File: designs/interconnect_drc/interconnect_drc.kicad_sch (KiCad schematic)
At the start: 1 part

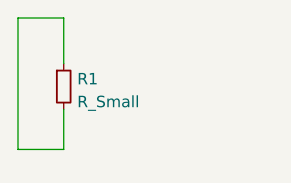
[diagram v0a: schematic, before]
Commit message: Convert to teardrop testcase
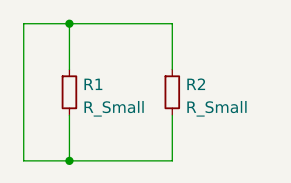
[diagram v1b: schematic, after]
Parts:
- added R2: R_Small, Resistor_SMD:R_0201_0603Metric_Pad0.64x0.40mm_HandSolder, symbol Device:R_Small
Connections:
- net at R1.1, R1.2: now also R2.1, R2.2
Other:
- moved on the sheet: R1
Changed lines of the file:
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@@
-(kicad_sch (version 20211123) (generator eeschema)
+(kicad_sch (version 20230121) (generator eeschema)
   (paper "A4")
-  (wire (pts (xy 93.345 112.395) (xy 93.345 127))
-    (stroke (width 0) (type default) (color 0 0 0 0))
+  (junction (at 99.06 113.03) (diameter 0) (color 0 0 0 0)
   )
-  (wire (pts (xy 98.425 117.475) (xy 98.425 112.395))
-    (stroke (width 0) (type default) (color 0 0 0 0))
+  (junction (at 99.06 128.27) (diameter 0) (color 0 0 0 0)
   )
-  (wire (pts (xy 98.425 112.395) (xy 93.345 112.395))
-    (stroke (width 0) (type default) (color 0 0 0 0))
+  (wire (pts (xy 99.06 113.03) (xy 110.49 113.03))
+    (stroke (width 0) (type default))
   )
-  (wire (pts (xy 98.425 127) (xy 98.425 122.555))
-    (stroke (width 0) (type default) (color 0 0 0 0))
+  (wire (pts (xy 110.49 123.19) (xy 110.49 128.27))
+    (stroke (width 0) (type default))
   )
-  (wire (pts (xy 93.345 127) (xy 98.425 127))
-    (stroke (width 0) (type default) (color 0 0 0 0))
+  (wire (pts (xy 110.49 128.27) (xy 99.06 128.27))
+    (stroke (width 0) (type default))
   )
-  (symbol (lib_id "Device:R_Small") (at 98.425 120.015 0) (unit 1)
-    (in_bom yes) (on_board yes) (fields_autoplaced)
-    (property "Reference" "R1" (id 0) (at 99.9236 119.1803 0)
+  (wire (pts (xy 110.49 113.03) (xy 110.49 118.11))
+    (stroke (width 0) (type default))
+  )
+  (wire (pts (xy 93.98 113.03) (xy 93.98 128.27))
+    (stroke (width 0) (type default))
+  )
+  (wire (pts (xy 99.06 118.11) (xy 99.06 113.03))
+    (stroke (width 0) (type default))
+  )
+  (wire (pts (xy 99.06 113.03) (xy 93.98 113.03))
+    (stroke (width 0) (type default))
+  )
+  (wire (pts (xy 99.06 128.27) (xy 99.06 123.19))
+    (stroke (width 0) (type default))
+  )
+  (wire (pts (xy 93.98 128.27) (xy 99.06 128.27))
+    (stroke (width 0) (type default))
+  )
+  (symbol (lib_id "Device:R_Small") (at 110.49 120.65 0) (unit 1)
+    (in_bom yes) (on_board yes) (dnp no) (fields_autoplaced)
+    (property "Reference" "R2" (at 111.9886 119.8153 0)
       (effects (font (size 1.27 1.27)) (justify left))
     )
-    (property "Value" "R_Small" (id 1) (at 99.9236 121.7172 0)
+    (property "Value" "R_Small" (at 111.9886 122.3522 0)
       (effects (font (size 1.27 1.27)) (justify left))
     )
-    (property "Footprint" "Resistor_SMD:R_0201_0603Metric_Pad0.64x0.40mm_HandSolder" (id 2) (at 98.425 120.015 0)
+    (property "Footprint" "Resistor_SMD:R_0201_0603Metric_Pad0.64x0.40mm_HandSolder" (at 110.49 120.65 0)
       (effects (font (size 1.27 1.27)) hide)
     )
-    (property "Datasheet" "~" (id 3) (at 98.425 120.015 0)
+    (property "Datasheet" "~" (at 110.49 120.65 0)
       (effects (font (size 1.27 1.27)) hide)
     )
     (pin "1")
     (pin "2")
+    (instances
+      (project "interconnect_drc"
+        (path "/0ce8ef0c-bf84-4f52-8da6-310f1efa5175"
+          (reference "R2") (unit 1)
+        )
+      )
+    )
+  )
+  (symbol (lib_id "Device:R_Small") (at 99.06 120.65 0) (unit 1)
+    (in_bom yes) (on_board yes) (dnp no) (fields_autoplaced)
+    (property "Reference" "R1" (at 100.5586 119.8153 0)
+      (effects (font (size 1.27 1.27)) (justify left))
+    )
+    (property "Value" "R_Small" (at 100.5586 122.3522 0)
+      (effects (font (size 1.27 1.27)) (justify left))
+    )
+    (property "Footprint" "Resistor_SMD:R_0201_0603Metric_Pad0.64x0.40mm_HandSolder" (at 99.06 120.65 0)
+      (effects (font (size 1.27 1.27)) hide)
+    )
+    (property "Datasheet" "~" (at 99.06 120.65 0)
+      (effects (font (size 1.27 1.27)) hide)
+    )
+    (pin "1")
+    (pin "2")
+    (instances
+      (project "interconnect_drc"
+        (path "/0ce8ef0c-bf84-4f52-8da6-310f1efa5175"
+          (reference "R1") (unit 1)
+        )
+      )
+    )
   )
   (sheet_instances
     (path "/" (page "1"))
   )
-  (symbol_instances
-    (path "/e656fc9e-6fc9-409b-980c-bf9cfe8c23a0"
-      (reference "R1") (unit 1) (value "R_Small") (footprint "Resistor_SMD:R_0201_0603Metric_Pad0.64x0.40mm_HandSolder")
-    )
-  )
 )

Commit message: Rename to tc6
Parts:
- removed R1, R2: R_Small, Resistor_SMD:R_0201_0603Metric_Pad0.64x0.40mm_HandSolder, symbol Device:R_Small
- added J9: Screw_Terminal_01x08, Project:TerminalBlock_Phoenix_MKDS_1727078_1x08_P3.81mm_Horizontal, symbol Connector:Screw_Terminal_01x08
- added R3: R_Small, Resistor_SMD:R_0805_2012Metric, symbol Device:R_Small
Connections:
- new net: J9.2 (Pin_2), J9.8 (Pin_8)
- new net: J9.3 (Pin_3), J9.4 (Pin_4)
- new net +3V3: R3.2
- new net GND: J9.1 (Pin_1), J9.5 (Pin_5), J9.7 (Pin_7), R3.1
